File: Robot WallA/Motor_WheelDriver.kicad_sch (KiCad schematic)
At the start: 24 parts, among them IC8 DRV8262DDVR, J15 39501-1002, J16 39501-1002, U4 125700D00000G, U5 125700D00000G

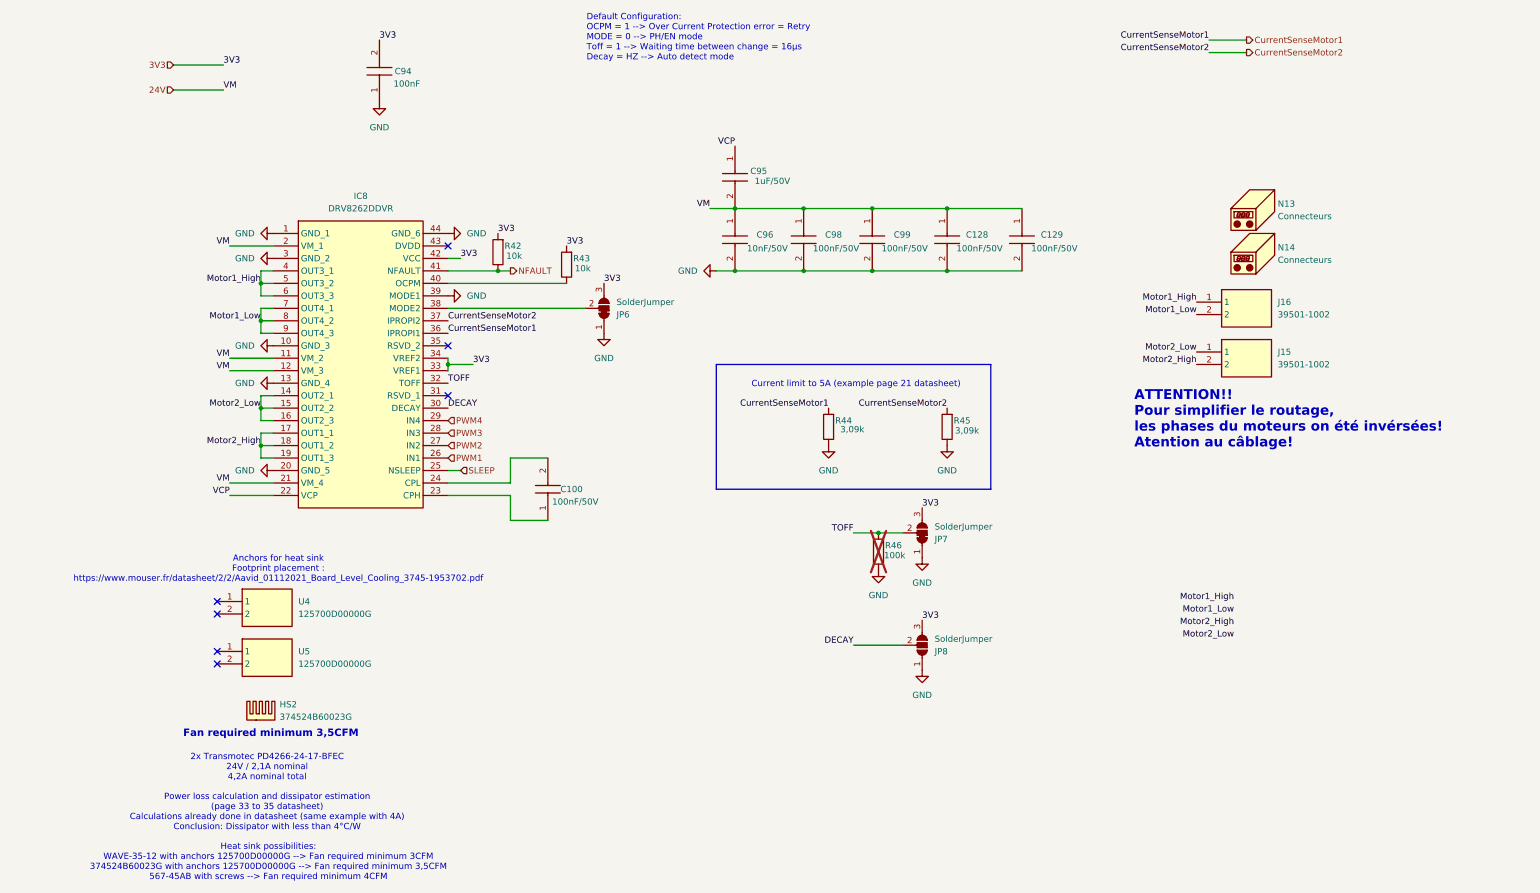
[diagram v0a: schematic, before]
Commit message: Modified a bit pin header pins to allow I2C,SPI and CAN
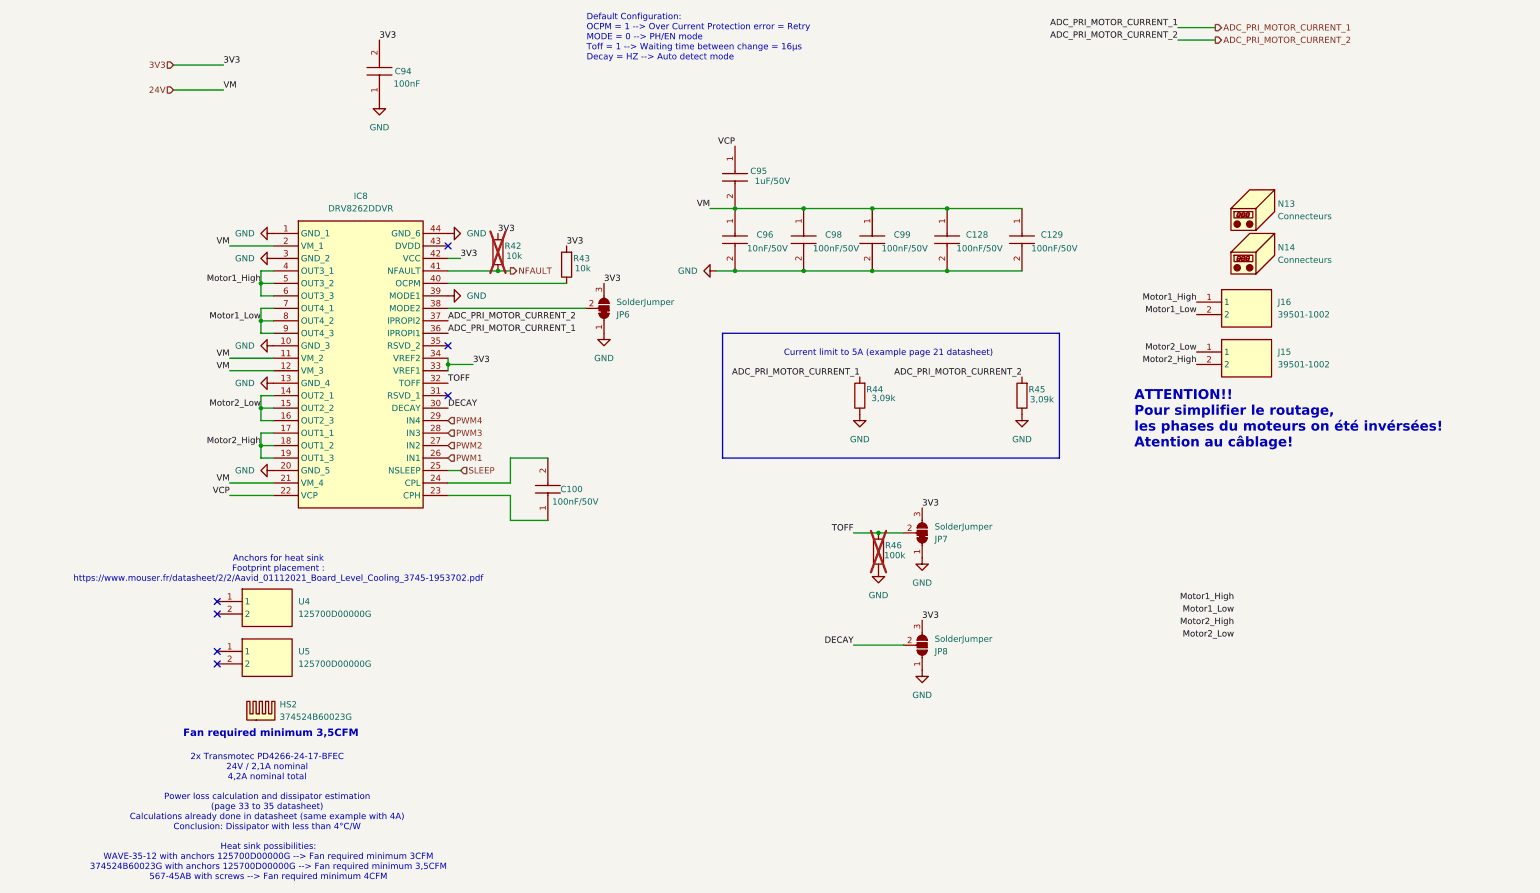
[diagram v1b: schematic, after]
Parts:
- R42: now not fitted
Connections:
- net CurrentSenseMotor1 renamed ADC_PRI_MOTOR_CURRENT_1
- net CurrentSenseMotor2 renamed ADC_PRI_MOTOR_CURRENT_2
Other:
- moved on the sheet: R44, R45
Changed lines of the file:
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@@
 	)
 	(rectangle
-		(start 151.13 88.9)
-		(end 207.01 114.3)
+		(start 152.4 82.55)
+		(end 220.98 107.95)
 		(stroke
 			(width 0)
@@
 	(text "Current limit to 5A (example page 21 datasheet)"
 		(exclude_from_sim no)
-		(at 179.578 92.964 0)
+		(at 186.182 86.614 0)
 		(effects
 			(font
@@
 	(wire
 		(pts
-			(xy 251.46 25.4) (xy 259.08 25.4)
+			(xy 245.11 22.86) (xy 252.73 22.86)
 		)
 		(stroke
@@
 	(wire
 		(pts
-			(xy 251.46 22.86) (xy 259.08 22.86)
+			(xy 245.11 20.32) (xy 252.73 20.32)
 		)
 		(stroke
@@
 		)
 	)
-	(label "CurrentSenseMotor2"
-		(at 251.46 25.4 180)
+	(label "ADC_PRI_MOTOR_CURRENT_2"
+		(at 245.11 22.86 180)
 		(effects
 			(font
@@
 		)
 	)
-	(label "CurrentSenseMotor1"
-		(at 251.46 22.86 180)
+	(label "ADC_PRI_MOTOR_CURRENT_1"
+		(at 245.11 20.32 180)
 		(effects
 			(font
@@
 		)
 	)
-	(label "CurrentSenseMotor1"
+	(label "ADC_PRI_MOTOR_CURRENT_1"
 		(at 96.52 82.55 0)
 		(effects
@@
 		)
 	)
-	(label "CurrentSenseMotor2"
+	(label "ADC_PRI_MOTOR_CURRENT_2"
 		(at 96.52 80.01 0)
 		(effects
@@
 		)
 	)
-	(label "CurrentSenseMotor2"
-		(at 198.12 97.79 180)
+	(label "ADC_PRI_MOTOR_CURRENT_2"
+		(at 213.36 91.44 180)
 		(effects
 			(font
@@
 		)
 	)
-	(label "CurrentSenseMotor1"
-		(at 173.99 97.79 180)
+	(label "ADC_PRI_MOTOR_CURRENT_1"
+		(at 180.34 91.44 180)
 		(effects
 			(font
@@
 		)
 	)
-	(hierarchical_label "CurrentSenseMotor2"
+	(hierarchical_label "ADC_PRI_MOTOR_CURRENT_2"
 		(shape output)
-		(at 259.08 25.4 0)
+		(at 252.73 22.86 0)
 		(effects
 			(font
@@
 		)
 	)
-	(hierarchical_label "CurrentSenseMotor1"
+	(hierarchical_label "ADC_PRI_MOTOR_CURRENT_1"
 		(shape output)
-		(at 259.08 22.86 0)
+		(at 252.73 20.32 0)
 		(effects
 			(font
@@
 	(symbol
 		(lib_id "Device:R")
-		(at 173.99 101.6 180)
+		(at 180.34 95.25 180)
 		(unit 1)
 		(exclude_from_sim no)
@@
 		(dnp no)
 		(property "Reference" "R44"
-			(at 177.038 100.33 0)
+			(at 183.388 93.98 0)
 			(effects
 				(font
@@
 		)
 		(property "Value" "3,09k"
-			(at 178.816 102.108 0)
+			(at 185.166 95.758 0)
 			(effects
 				(font
@@
 		)
 		(property "Footprint" "Resistor_SMD:R_0603_1608Metric_Pad0.98x0.95mm_HandSolder"
-			(at 175.768 101.6 90)
+			(at 182.118 95.25 90)
 			(effects
 				(font
@@
 		)
 		(property "Datasheet" "~"
-			(at 173.99 101.6 0)
+			(at 180.34 95.25 0)
 			(effects
 				(font
@@
 		)
 		(property "Description" "Resistor"
-			(at 173.99 101.6 0)
+			(at 180.34 95.25 0)
 			(effects
 				(font
@@
 	(symbol
 		(lib_id "Device:R")
-		(at 198.12 101.6 180)
+		(at 213.36 95.25 180)
 		(unit 1)
 		(exclude_from_sim no)
@@
 		(dnp no)
 		(property "Reference" "R45"
-			(at 201.168 100.33 0)
+			(at 216.408 93.98 0)
 			(effects
 				(font
@@
 		)
 		(property "Value" "3,09k"
-			(at 202.184 102.362 0)
+			(at 217.424 96.012 0)
 			(effects
 				(font
@@
 		)
 		(property "Footprint" "Resistor_SMD:R_0603_1608Metric_Pad0.98x0.95mm_HandSolder"
-			(at 199.898 101.6 90)
+			(at 215.138 95.25 90)
 			(effects
 				(font
@@
 		)
 		(property "Datasheet" "~"
-			(at 198.12 101.6 0)
+			(at 213.36 95.25 0)
 			(effects
 				(font
@@
 		)
 		(property "Description" "Resistor"
-			(at 198.12 101.6 0)
+			(at 213.36 95.25 0)
 			(effects
 				(font
@@
 	(symbol
 		(lib_id "power:GND")
-		(at 173.99 105.41 0)
+		(at 180.34 99.06 0)
 		(unit 1)
 		(exclude_from_sim no)
@@
 		(fields_autoplaced yes)
 		(property "Reference" "#PWR0101"
-			(at 173.99 111.76 0)
+			(at 180.34 105.41 0)
 			(effects
 				(font
@@
 		)
 		(property "Value" "GND"
-			(at 173.99 110.49 0)
+			(at 180.34 104.14 0)
 			(effects
 				(font
@@
 		)
 		(property "Footprint" ""
-			(at 173.99 105.41 0)
+			(at 180.34 99.06 0)
 			(effects
 				(font
@@
 		)
 		(property "Datasheet" ""
-			(at 173.99 105.41 0)
+			(at 180.34 99.06 0)
 			(effects
 				(font
@@
 		)
 		(property "Description" "Power symbol creates a global label with name \"GND\" , ground"
-			(at 173.99 105.41 0)
+			(at 180.34 99.06 0)
 			(effects
 				(font
@@
 		(in_bom yes)
 		(on_board yes)
-		(dnp no)
+		(dnp yes)
 		(property "Reference" "R42"
 			(at 109.728 64.77 0)
@@
 	(symbol
 		(lib_id "power:GND")
-		(at 198.12 105.41 0)
+		(at 213.36 99.06 0)
 		(unit 1)
 		(exclude_from_sim no)
@@
 		(fields_autoplaced yes)
 		(property "Reference" "#PWR0102"
-			(at 198.12 111.76 0)
+			(at 213.36 105.41 0)
 			(effects
 				(font
@@
 		)
 		(property "Value" "GND"
-			(at 198.12 110.49 0)
+			(at 213.36 104.14 0)
 			(effects
 				(font
@@
 		)
 		(property "Footprint" ""
-			(at 198.12 105.41 0)
+			(at 213.36 99.06 0)
 			(effects
 				(font
@@
 		)
 		(property "Datasheet" ""
-			(at 198.12 105.41 0)
+			(at 213.36 99.06 0)
 			(effects
 				(font
@@
 		)
 		(property "Description" "Power symbol creates a global label with name \"GND\" , ground"
-			(at 198.12 105.41 0)
+			(at 213.36 99.06 0)
 			(effects
 				(font

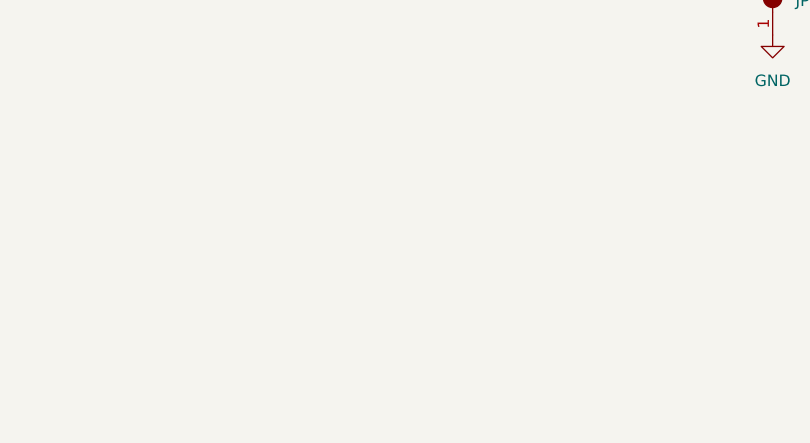
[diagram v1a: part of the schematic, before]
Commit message: Added 3 thermistor to measure temperature near 12V and 24V power supplies and near motor drivers
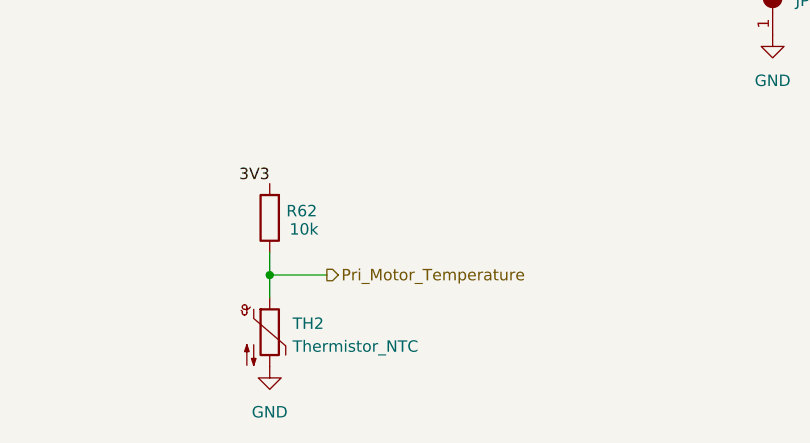
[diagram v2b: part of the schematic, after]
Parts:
- added R62: 10k, Resistor_SMD:R_0603_1608Metric_Pad0.98x0.95mm_HandSolder, symbol Device:R
- added TH2: Thermistor_NTC, Resistor_SMD:R_0603_1608Metric_Pad0.98x0.95mm_HandSolder, symbol Device:Thermistor_NTC
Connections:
- net 3V3: now also R62.2
- net GND: now also TH2.2
- new net Pri_Motor_Temperature: R62.1, TH2.1

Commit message: Modified footprint to simplify BOM. Finalized BOM.
Updated fab files
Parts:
- removed C96: 10nF/50V, Capacitor_SMD:C_0603_1608Metric_Pad1.08x0.95mm_HandSolder, symbol SamacSys_Parts:0805DC104MAT2A
- added C96: 10nF/50V, Capacitor_SMD:C_0805_2012Metric_Pad1.18x1.45mm_HandSolder, symbol Device:C
- C100, C128, C129, C94, C98, C99: Manufacturer_Part_Number (none) -> KGM15BR71H104KT
- C95: Manufacturer_Part_Number (none) -> CL10A105KB8NNNC
- R42, R43, R62: Manufacturer_Part_Number (none) -> 667-ERJ-3GEYJ103V
- R44, R45: Manufacturer_Part_Number (none) -> CRCW06033K09FKEA
- R46: Manufacturer_Part_Number (none) -> RCA0603100KFKEAHP
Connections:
- net 24V: now also C96.1
- net GND: now also C96.2

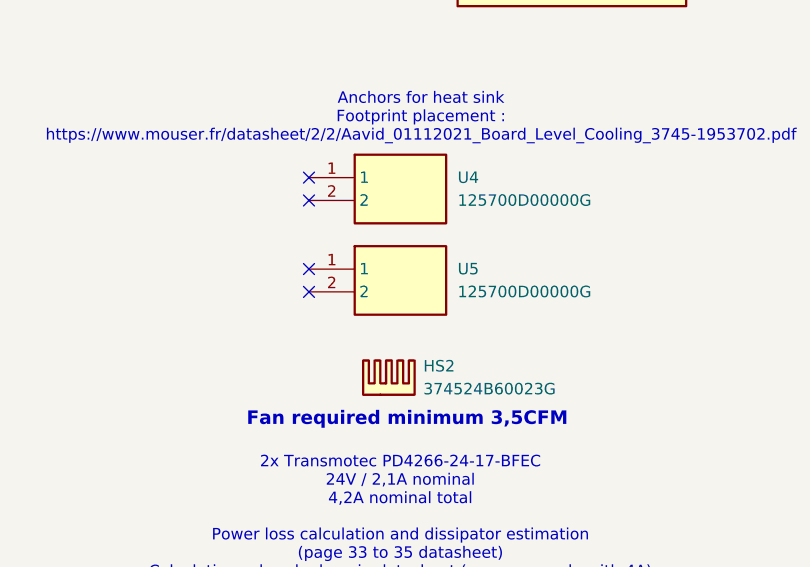
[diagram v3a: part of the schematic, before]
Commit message: Added Thermal pads for heatsinks in BOM.
Updated fab files
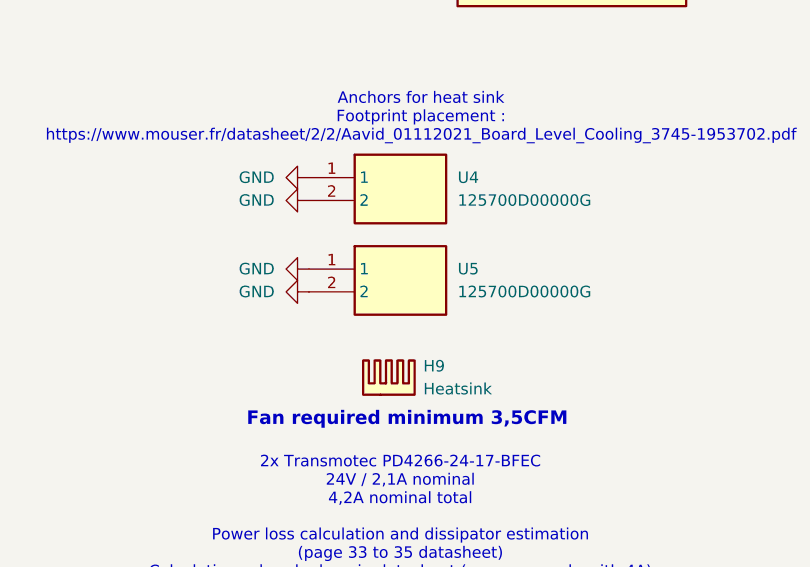
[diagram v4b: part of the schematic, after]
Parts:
- H9: renamed from HS2; value 374524B60023G -> Heatsink
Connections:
- net GND: now also U4.1, U4.2, U5.1, U5.2
- no-connect marks 7 -> 3
